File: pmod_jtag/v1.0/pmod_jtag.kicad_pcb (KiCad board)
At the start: 2 copper layers, 20 x 15.5 mm, 70 parts, among them J1 pkl_jumper, J2 pkl_jumper, J3 pkl_jumper, J4 CONN_02X06, SW1 TACT, X1 JTAG-10

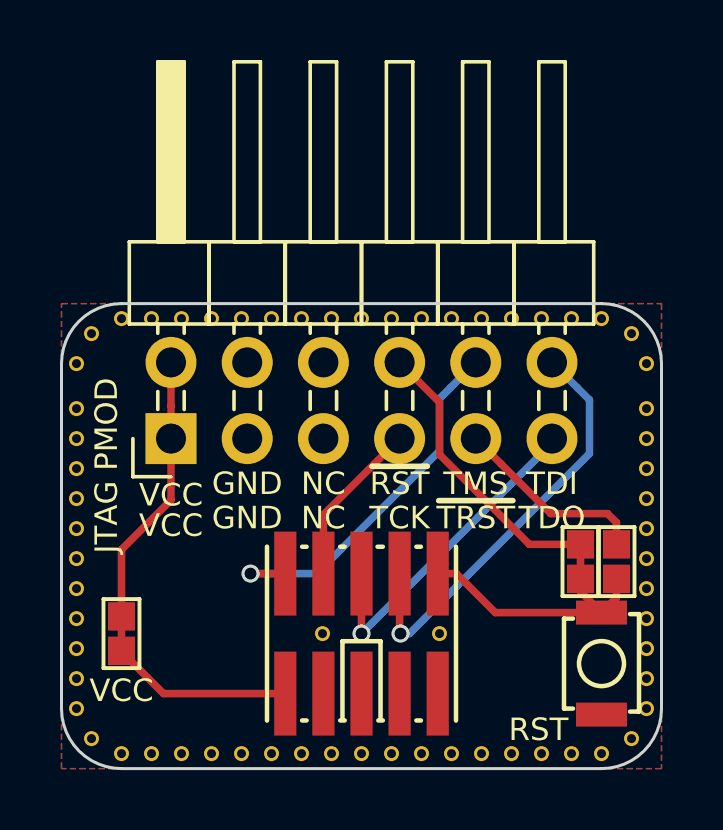
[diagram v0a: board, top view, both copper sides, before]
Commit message: Added pin 1 indicator on the 10pin connector.
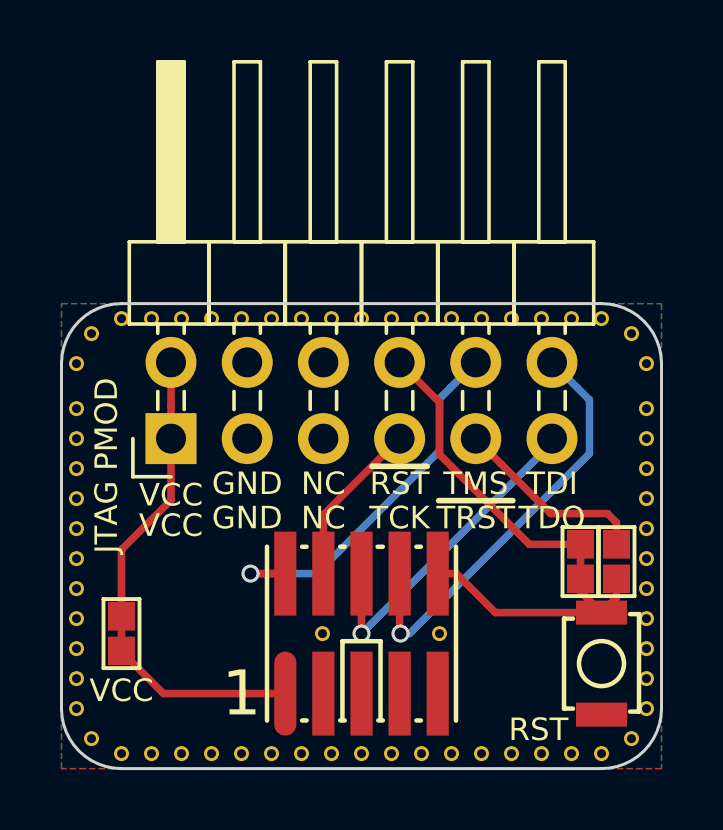
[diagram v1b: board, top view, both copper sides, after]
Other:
- board text added: "1"
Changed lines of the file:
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@@
-(kicad_pcb (version 4) (host pcbnew 4.0.6-e0-6349~53~ubuntu16.04.1)
+(kicad_pcb (version 4) (host pcbnew 4.0.7-e2-6376~58~ubuntu16.04.1)
   (general
     (links 83)
@@
     (area 19.922025 21.074999 52.85 51.7)
     (thickness 1.6)
-    (drawings 45)
+    (drawings 46)
     (tracks 47)
     (zones 0)
@@
     (mod_text_size 1 1)
     (mod_text_width 0.15)
-    (pad_size 2.032 1.7272)
-    (pad_drill 1.016)
+    (pad_size 0.74 2.8)
+    (pad_drill 0)
     (pad_to_mask_clearance 0)
     (aux_axis_origin 0 0)
@@
       (drillshape 0)
       (scaleselection 1)
-      (outputdirectory gerber))
+      (outputdirectory pmod_jtag_gerber))
   )
   (net 0 "")
@@
     (fp_line (start 3.15 2.9) (end 3.15 -2.9) (layer F.SilkS) (width 0.15))
     (fp_line (start -3.15 2.9) (end -3.15 -2.9) (layer F.SilkS) (width 0.15))
-    (pad 1 smd rect (at 2.54 -2) (size 0.74 2.8) (layers F.Cu F.Paste F.Mask)
+    (pad 1 smd oval (at 2.54 -2) (size 0.74 2.8) (layers F.Cu F.Paste F.Mask)
       (net 4 /VCC))
     (pad 2 smd rect (at 2.54 2) (size 0.74 2.8) (layers F.Cu F.Paste F.Mask)
@@
       (net 8 /TRST))
   )
+  (gr_text 1 (at 26 42.5) (layer F.SilkS)
+    (effects (font (size 1.5 1.5) (thickness 0.3)))
+  )
   (gr_text VCC (at 22 42.4) (layer F.SilkS)
